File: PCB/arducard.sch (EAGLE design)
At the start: 88 parts, among them J1 USB MICRO, Q1 BC817-16LT1SMD, Q2 DMG2301U-7, Q3 2N7002, Q4 BSS84, Q5 2N7002, Q6 2N7002, Q7 2N7002, Q8 BSS84, Q9 DMG2301U-7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

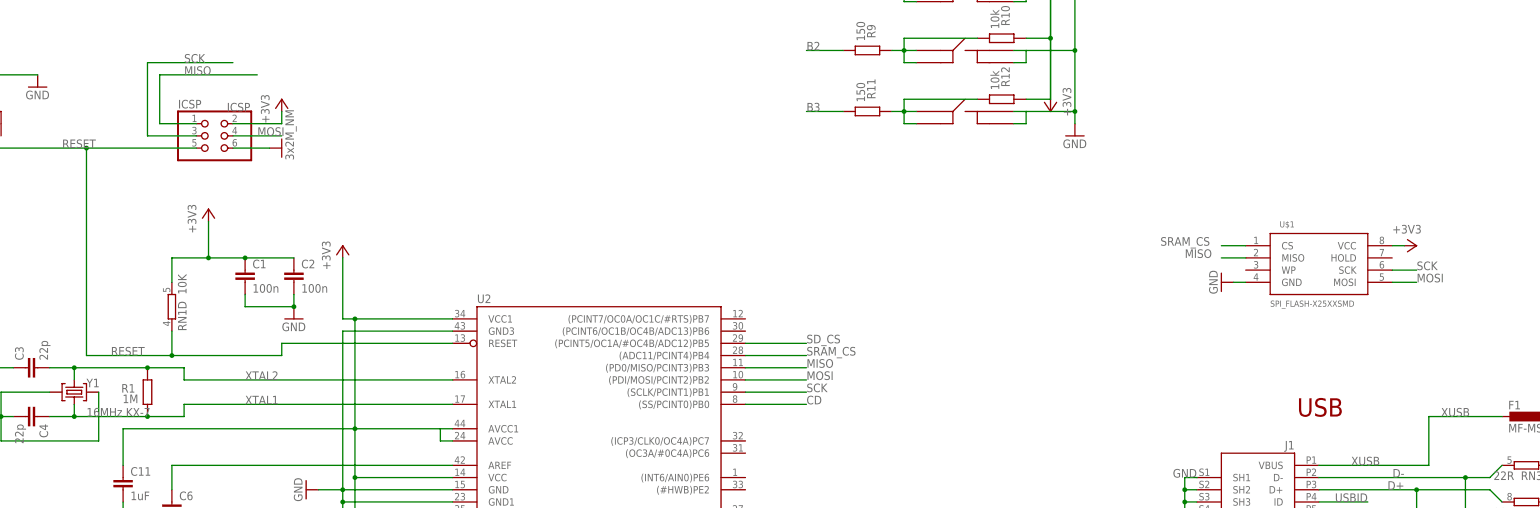
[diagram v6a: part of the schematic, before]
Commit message: changed SRAM to FRAM
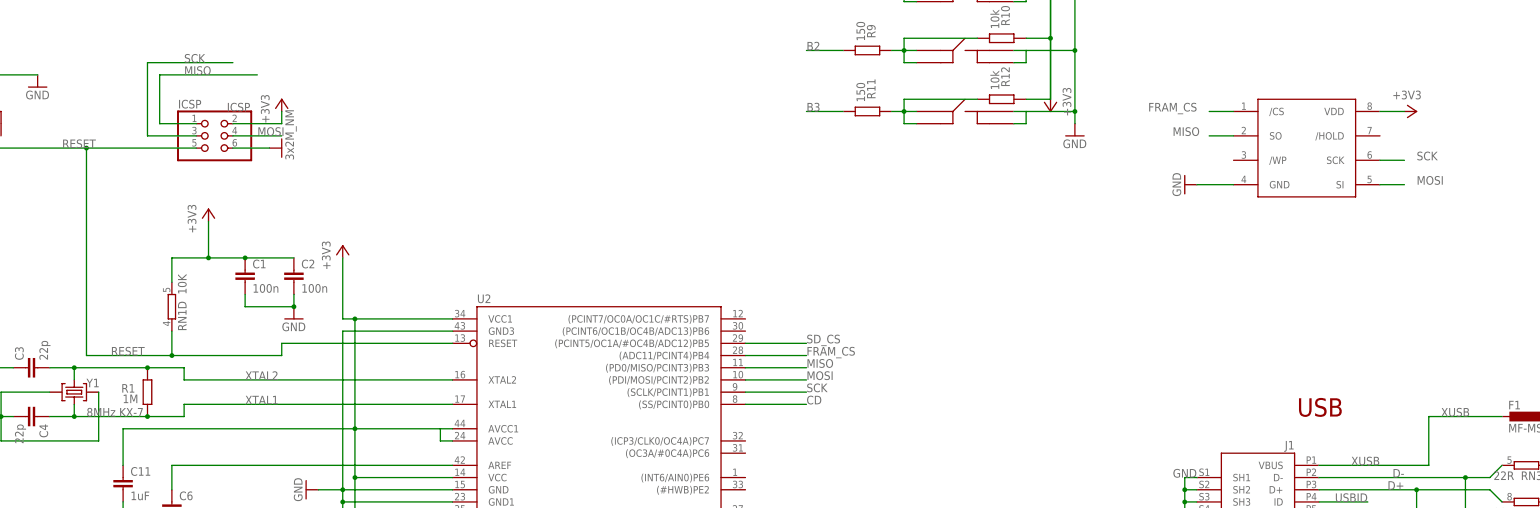
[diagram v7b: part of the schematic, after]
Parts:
- removed U$1: SPI_FLASH-X25XXSMD, SparkFun-DigitalIC:SPI_FLASH-X25XXSMD
- added U$5: MB85RS128B-FRAM, arducard-fram:MB85RS128B-FRAM
- Y1: value 16MHz KX-7 -> 8MHz KX-7
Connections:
- removed net SRAM_CS: U$1.CS, U2.(ADC11/PCINT4)PB4
- new net FRAM_CS: U$5./CS, U2.(ADC11/PCINT4)PB4
- net +3V3: now also U$5.VDD; no longer U$1.VCC
- net GND: now also U$5.GND; no longer U$1.GND
- net MISO: now also U$5.SO; no longer U$1.MISO
- net MOSI: now also U$5.SI; no longer U$1.MOSI
- net SCK: now also U$5.SCK; no longer U$1.SCK
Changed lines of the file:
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@@
 <part name="GND18" library="supply1" deviceset="GND" device=""/>
 <part name="RN1" library="resistor-dil" deviceset="4R-N" device="CAY16" value="10K"/>
-<part name="Y1" library="SmartPrj" deviceset="CRYSTAL-3.2-2.5" device="" value="16MHz KX-7"/>
+<part name="Y1" library="SmartPrj" deviceset="CRYSTAL-3.2-2.5" device="" value="8MHz KX-7"/>
 <part name="F1" library="rcl" deviceset="L-EU" device="L1812" value="MF-MSMF050-2 500mA"/>
 <part name="Z1" library="varistor" deviceset="VARISTOR" device="CN0603" value="CG0603MLC-05E"/>
@@
 <part name="J1" library="SmartPrj" deviceset="MYCON2_USB-MINI-B" device="" value="USB MICRO"/>
 <part name="GND2" library="supply1" deviceset="GND" device=""/>
-<part name="U$1" library="SparkFun-DigitalIC" deviceset="SPI_FLASH-X25XX" device="SMD"/>
 <part name="+3V1" library="supply1" deviceset="+3V3" device=""/>
 <part name="+3V2" library="supply1" deviceset="+3V3" device=""/>
@@
 <part name="GND4" library="supply1" deviceset="GND" device=""/>
 <part name="GND29" library="supply1" deviceset="GND" device=""/>
+<part name="U$5" library="arducard-fram" deviceset="MB85RS128B-FRAM" device=""/>
 </parts>
 <sheets>
@@
 <instance part="J1" gate="G$1" x="279.4" y="88.9" rot="MR0"/>
 <instance part="GND2" gate="1" x="307.34" y="35.56"/>
-<instance part="U$1" gate="G$1" x="292.1" y="137.16"/>
 <instance part="+3V1" gate="G$1" x="60.96" y="147.32"/>
 <instance part="+3V2" gate="G$1" x="88.9" y="139.7"/>
-<instance part="+3V3" gate="G$1" x="312.42" y="139.7" rot="R270"/>
+<instance part="+3V3" gate="G$1" x="312.42" y="167.64" rot="R270"/>
 <instance part="U2" gate="G$1" x="137.16" y="101.6"/>
 <instance part="U1" gate="G$1" x="358.14" y="144.78" smashed="yes" rot="MR0">
@@
 <instance part="C11" gate="G$1" x="43.18" y="91.44"/>
 <instance part="GND3" gate="1" x="43.18" y="81.28"/>
-<instance part="GND5" gate="1" x="271.78" y="132.08" rot="R270"/>
+<instance part="GND5" gate="1" x="264.16" y="152.4" rot="R270"/>
 <instance part="GND6" gate="1" x="241.3" y="162.56"/>
 <instance part="GND7" gate="1" x="373.38" y="121.92"/>
@@
 <instance part="GND4" gate="1" x="81.28" y="88.9" rot="R270"/>
 <instance part="GND29" gate="1" x="78.74" y="124.46"/>
+<instance part="U$5" gate="G$1" x="289.56" y="162.56"/>
 </instances>
 <busses>
@@
 </segment>
 <segment>
-<pinref part="U$1" gate="G$1" pin="GND"/>
-<wire x1="276.86" y1="132.08" x2="274.32" y2="132.08" width="0.1524" layer="91"/>
+<wire x1="274.32" y1="152.4" x2="266.7" y2="152.4" width="0.1524" layer="91"/>
 <pinref part="GND5" gate="1" pin="GND"/>
+<pinref part="U$5" gate="G$1" pin="GND"/>
 </segment>
 <segment>
@@
 </segment>
 <segment>
-<pinref part="U$1" gate="G$1" pin="SCK"/>
-<wire x1="307.34" y1="134.62" x2="312.42" y2="134.62" width="0.1524" layer="91"/>
-<label x="312.42" y="134.62" size="1.778" layer="95"/>
+<wire x1="304.8" y1="157.48" x2="309.88" y2="157.48" width="0.1524" layer="91"/>
+<label x="312.42" y="157.48" size="1.778" layer="95"/>
+<pinref part="U$5" gate="G$1" pin="SCK"/>
 </segment>
 <segment>
@@
 </segment>
 <segment>
-<pinref part="U$1" gate="G$1" pin="MISO"/>
-<wire x1="276.86" y1="137.16" x2="271.78" y2="137.16" width="0.1524" layer="91"/>
-<label x="264.16" y="137.16" size="1.778" layer="95"/>
+<wire x1="274.32" y1="162.56" x2="269.24" y2="162.56" width="0.1524" layer="91"/>
+<label x="261.62" y="162.56" size="1.778" layer="95"/>
+<pinref part="U$5" gate="G$1" pin="SO"/>
 </segment>
 <segment>
@@
 </segment>
 <segment>
-<pinref part="U$1" gate="G$1" pin="MOSI"/>
-<wire x1="307.34" y1="132.08" x2="312.42" y2="132.08" width="0.1524" layer="91"/>
-<label x="312.42" y="132.08" size="1.778" layer="95"/>
+<wire x1="304.8" y1="152.4" x2="309.88" y2="152.4" width="0.1524" layer="91"/>
+<label x="312.42" y="152.4" size="1.778" layer="95"/>
+<pinref part="U$5" gate="G$1" pin="SI"/>
 </segment>
 <segment>
@@
 </segment>
 <segment>
-<pinref part="U$1" gate="G$1" pin="VCC"/>
-<wire x1="307.34" y1="139.7" x2="309.88" y2="139.7" width="0.1524" layer="91"/>
+<wire x1="304.8" y1="167.64" x2="309.88" y2="167.64" width="0.1524" layer="91"/>
 <pinref part="+3V3" gate="G$1" pin="+3V3"/>
+<pinref part="U$5" gate="G$1" pin="VDD"/>
 </segment>
 <segment>
@@
 </segment>
 </net>
-<net name="SRAM_CS" class="0">
-<segment>
-<pinref part="U$1" gate="G$1" pin="CS"/>
-<wire x1="276.86" y1="139.7" x2="271.78" y2="139.7" width="0.1524" layer="91"/>
-<label x="259.08" y="139.7" size="1.778" layer="95"/>
-</segment>
-<segment>
+<net name="FRAM_CS" class="0">
+<segment>
+<wire x1="274.32" y1="167.64" x2="269.24" y2="167.64" width="0.1524" layer="91"/>
+<label x="256.54" y="167.64" size="1.778" layer="95"/>
+<pinref part="U$5" gate="G$1" pin="/CS"/>
+</segment>
+<segment>

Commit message: added 5th button
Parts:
- removed RN1: 10K, resistor-dil:4R-NCAY16
- removed RN3: 22R, resistor-dil:4R-NCAY16
- added R14, R4: 22R, SmartPrj:R-EU_R0603
- added R26: 150, SmartPrj:R-EU_R0603
- added R27, R3: 10k, SmartPrj:R-EU_R0603
- added U$1: EVQ-PUA, arducard-switch:EVQ-PUA
- C8: device rcl:CPOL-EUSMCB -> SmartPrj:C-EUC0603
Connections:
- removed net BATTSTAT1: U2.(ADC0)PF0
- removed net BATTSTAT2: U2.(ADC1)PF1
- removed net CD: R13.2, U2.(SS/PCINT0)PB0
- removed net N$17: R19.1, U4.INT/SQW
- removed net N$4: U$3./CHG
- new net B4: R26.1, U2.(PCINT7/OC0A/OC1C/#RTS)PB7
- new net CHGSTAT: U$3./CHG, U2.(ADC6/TDO)PF6
- new net N$8: R26.2, R27.1, U$1.1, U$1.3
- new net RTC_INT: R19.1, U2.(PCINT6/OC1B/OC4B/ADC13)PB6, U4.INT/SQW
- new net SD_CD: R13.2, U2.(PCINT5/OC1A/#OC4B/ADC12)PB5
- net +3V3: now also R3.2, U$1.2, U$1.4, U$11.2, U$11.4, U$14.2, U$14.4, U$8.2, U$8.4, U$9.2, U$9.4; no longer R10.2, R12.2, R6.2, R8.2, RN1D.2
- net D+: now also R4.1; no longer RN3A.2
- net D-: now also R14.1; no longer RN3D.2
- net EPD_CS: now also U2.(T0/OC4D/ADC10)PD7
- net FRAM_CS: now also U2.(ICP1/ADC8)PD4; no longer U2.(ADC11/PCINT4)PB4
- net GND: now also C8.1, R10.2, R12.2, R27.2, R6.2, R8.2; no longer C8.-, U$11.2, U$11.4, U$14.2, U$14.4, U$8.2, U$8.4, U$9.2, U$9.4
- net RD+: now also R4.2; no longer RN3A.1
- net RD-: now also R14.2; no longer RN3D.1
- net RESET: now also R3.1; no longer RN1D.1
- net RTC_CS: now also U2.(T1/#OC4D/ADC9)PD6
- net SD_CS: now also U2.(XCK1/#CTS)PD5; no longer U2.(PCINT5/OC1A/#OC4B/ADC12)PB5
- net VUSB: now also C8.2; no longer C8.+
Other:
- moved on the sheet: F1, R15, R19
